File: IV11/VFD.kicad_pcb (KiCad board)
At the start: 2 copper layers, 225 x 80 mm, 71 parts, among them J1 USB_B, SW1 switch, SW2 switch, SW3 switch, SW4 switch, U1 74HC595, U10 UDN2981, U11 UDN2981, U12 UDN2981, U13 WeMos_mini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

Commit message: Changes for back to front LED markings
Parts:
- moved D6 4.07 mm to (154.7, 37.8), turned to 270 degrees
- moved D4 3.96 mm to (98.7, 38.0), turned to 270 degrees
- moved D8 3.96 mm to (211.2, 38.0), turned to 270 degrees
- moved D5 3.95 mm to (126.6, 41.8), turned to 90 degrees
- moved D3 3.81 mm to (70.2, 41.9), turned to 90 degrees
- moved D2 3.81 mm to (42.2, 38.1), turned to 270 degrees
- moved D1 3.78 mm to (14.0, 41.8), turned to 90 degrees
- moved D7 3.49 mm to (182.9, 41.9), turned to 90 degrees
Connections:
- D1 pad 1: LED_DATA_IN -> Net-(D1-Pad1)
- D1 pad 2: Net-(D1-Pad2) -> GND
- D1 pad 3: GND -> Net-(D1-Pad3)
- D1 pad 4: Net-(D1-Pad4) -> LED_DATA_IN
- D2 pad 1: Net-(D1-Pad4) -> Net-(D2-Pad1)
- D2 pad 2: +5V -> Net-(D2-Pad2)
- D2 pad 3: GND -> Net-(D2-Pad3)
- D2 pad 4: Net-(D2-Pad4) -> Net-(D1-Pad1)
- D3 pad 1: Net-(D2-Pad4) -> Net-(D3-Pad1)
- D3 pad 2: +5V -> Net-(D3-Pad2)
- D3 pad 3: GND -> Net-(D3-Pad3)
- D3 pad 4: Net-(D3-Pad4) -> Net-(D2-Pad1)
- D4 pad 1: Net-(D3-Pad4) -> Net-(D4-Pad1)
- D4 pad 2: +5V -> GND
- D4 pad 3: GND -> Net-(D4-Pad3)
- D4 pad 4: Net-(D4-Pad4) -> Net-(D3-Pad1)
- D5 pad 1: Net-(D4-Pad4) -> Net-(D5-Pad1)
- D5 pad 2: +5V -> GND
- D5 pad 3: GND -> +5V
- D5 pad 4: Net-(D5-Pad4) -> Net-(D4-Pad1)
- D6 pad 1: Net-(D5-Pad4) -> Net-(D6-Pad1)
- D6 pad 2: +5V -> Net-(D6-Pad2)
- D6 pad 3: GND -> Net-(D6-Pad3)
- D6 pad 4: Net-(D6-Pad4) -> Net-(D5-Pad1)
- D7 pad 1: Net-(D6-Pad4) -> Net-(D7-Pad1)
- D7 pad 2: +5V -> Net-(D7-Pad2)
- D7 pad 3: GND -> Net-(D7-Pad3)
- D7 pad 4: Net-(D7-Pad4) -> Net-(D6-Pad1)
- D8 pad 1: Net-(D7-Pad4) -> LED_DATA_OUT
- D8 pad 2: +5V -> GND
- D8 pad 3: GND -> Net-(D8-Pad3)
- D8 pad 4: LED_DATA_OUT -> Net-(D7-Pad1)
- D9 pad 1: Net-(D1-Pad2) -> Net-(D1-Pad3)
- SW2 pad 2: GND -> Net-(SW2-Pad2)
- SW3 pad 2: GND -> Net-(SW3-Pad2)
- SW4 pad 2: GND -> Net-(SW4-Pad2)
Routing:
- net Net-(D6-Pad4): track 30.3 -> 0.00 mm
- net Net-(D6-Pad1): track 0.00 -> 30.3 mm
- net Net-(D5-Pad4): track 29.9 -> 0.00 mm
- net Net-(D5-Pad1): track 0.00 -> 29.9 mm
- net Net-(D2-Pad4): track 29.7 -> 0.00 mm
- net Net-(D2-Pad1): track 0.00 -> 29.7 mm
- net Net-(D1-Pad4): track 29.3 -> 0.00 mm
- net Net-(D1-Pad1): track 0.00 -> 29.3 mm
- net Net-(D7-Pad4): track 29.3 -> 0.00 mm
- net Net-(D7-Pad1): track 0.00 -> 29.3 mm
- net Net-(D3-Pad4): track 29.1 -> 0.00 mm
- net Net-(D3-Pad1): track 0.00 -> 29.1 mm
- net Net-(D4-Pad4): track 29.1 -> 0.00 mm
- net Net-(D4-Pad1): track 0.00 -> 29.1 mm
- net Net-(D1-Pad3): track 0.00 -> 14.8 mm, vias 0 -> 1
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
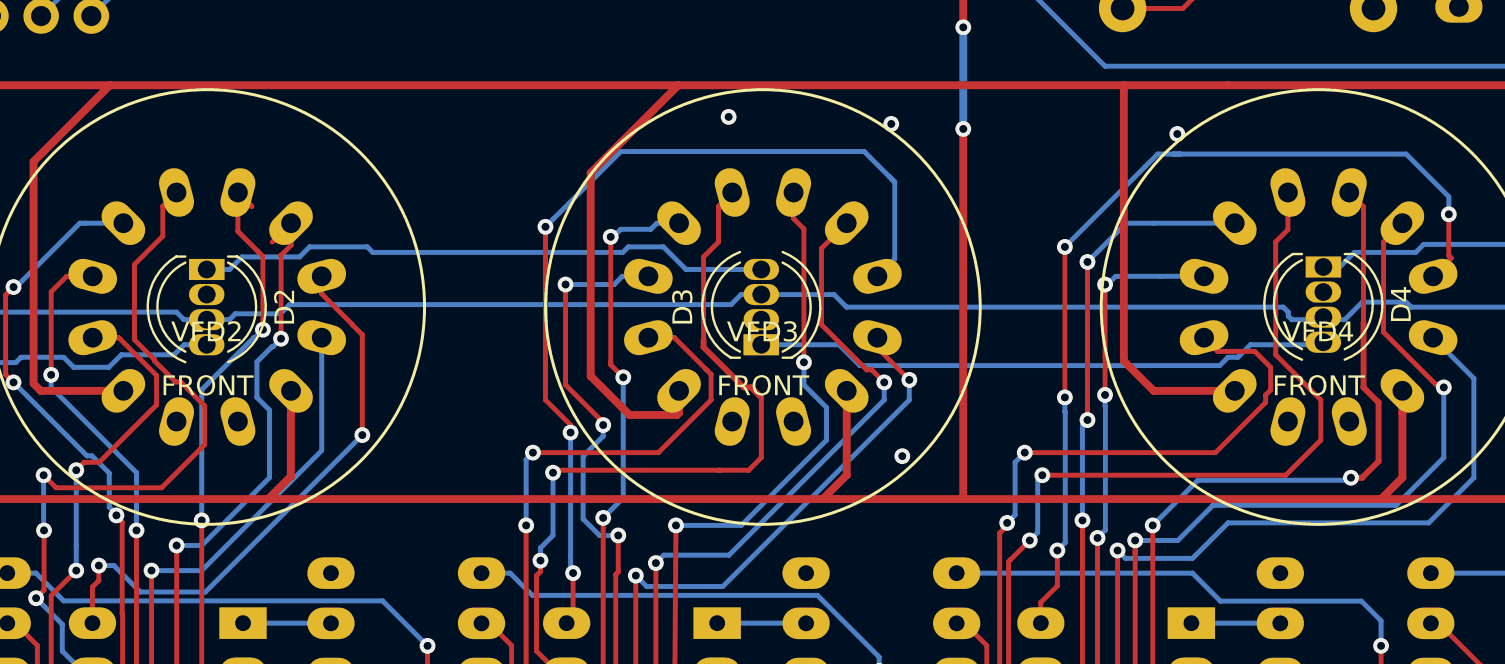
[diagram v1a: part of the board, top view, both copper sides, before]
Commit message: Fix footpring mistakes
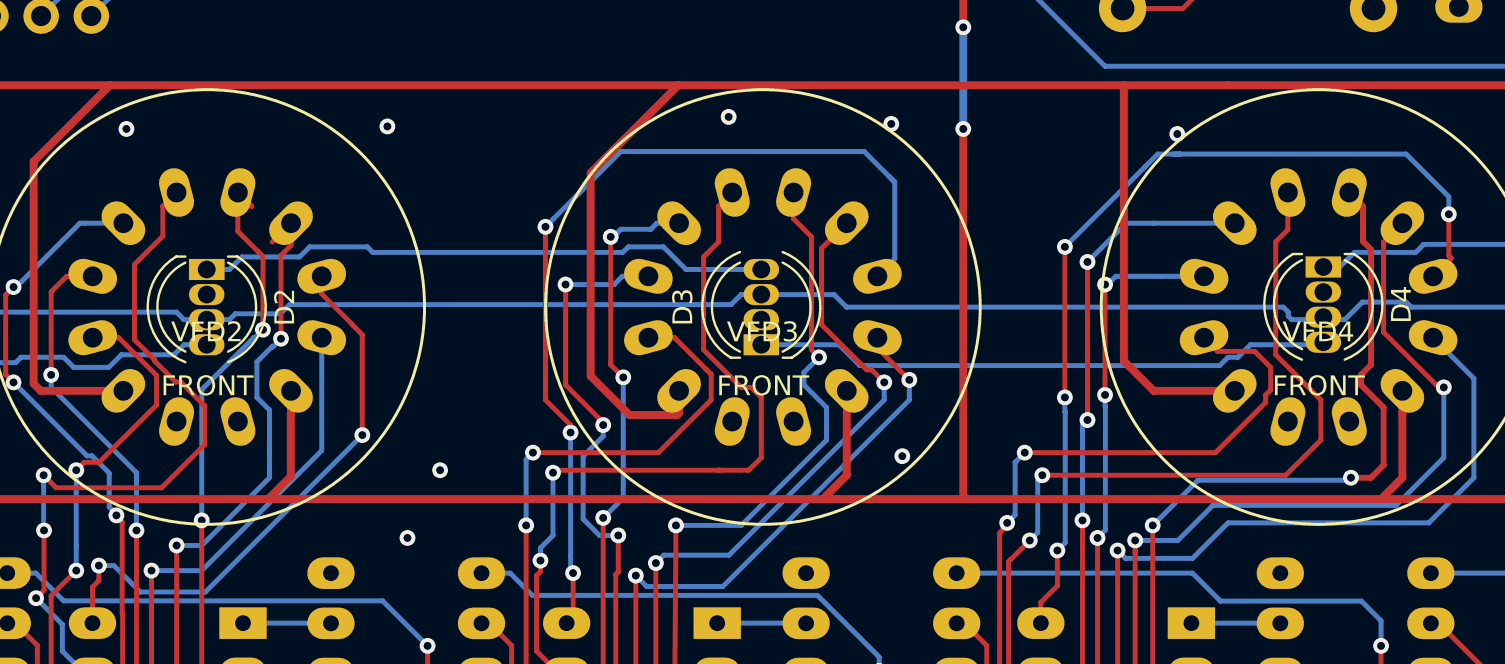
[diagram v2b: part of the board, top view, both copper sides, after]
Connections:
- C1 pad 1: VCC -> +3V3
- C2 pad 1: VCC -> +3V3
- C3 pad 1: VCC -> +3V3
- C4 pad 1: VCC -> +3V3
- C5 pad 1: VCC -> +3V3
- C6 pad 1: VCC -> +3V3
- C7 pad 1: VCC -> +3V3
- C8 pad 1: VCC -> +3V3
- D3 pad 2: Net-(D3-Pad2) -> GND
- D3 pad 3: Net-(D3-Pad3) -> +5V
- D4 pad 3: Net-(D4-Pad3) -> +5V
- D6 pad 2: Net-(D6-Pad2) -> GND
- D6 pad 3: Net-(D6-Pad3) -> +5V
- U1 pad 10: VCC -> +3V3
- U1 pad 16: VCC -> +3V3
- U14 pad 10: VCC -> +3V3
- U14 pad 16: VCC -> +3V3
- U15 pad 10: VCC -> +3V3
- U15 pad 16: VCC -> +3V3
- U2 pad 10: VCC -> +3V3
- U2 pad 16: VCC -> +3V3
- U3 pad 10: VCC -> +3V3
- U3 pad 16: VCC -> +3V3
- U7 pad 10: VCC -> +3V3
- U7 pad 16: VCC -> +3V3
- U8 pad 10: VCC -> +3V3
- U8 pad 16: VCC -> +3V3
- U9 pad 10: VCC -> +3V3
- U9 pad 16: VCC -> +3V3
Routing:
- net VCC: track 411.5 -> 0.00 mm
- net +3V3: track 260.0 -> 671.4 mm
- net Net-(U5-Pad11): track 49.4 -> 51.4 mm
- net Net-(U11-Pad11): track 52.9 -> 53.8 mm
- net GND: vias 19 -> 23

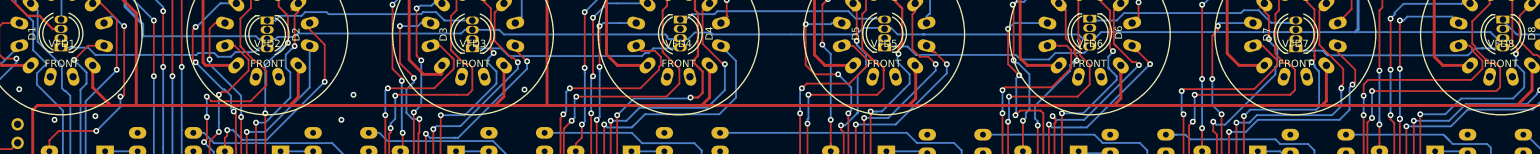
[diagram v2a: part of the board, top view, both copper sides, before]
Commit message: Update footprints to use the 'generic modules'
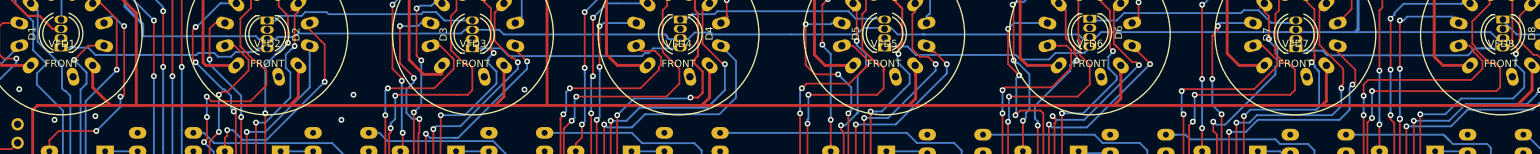
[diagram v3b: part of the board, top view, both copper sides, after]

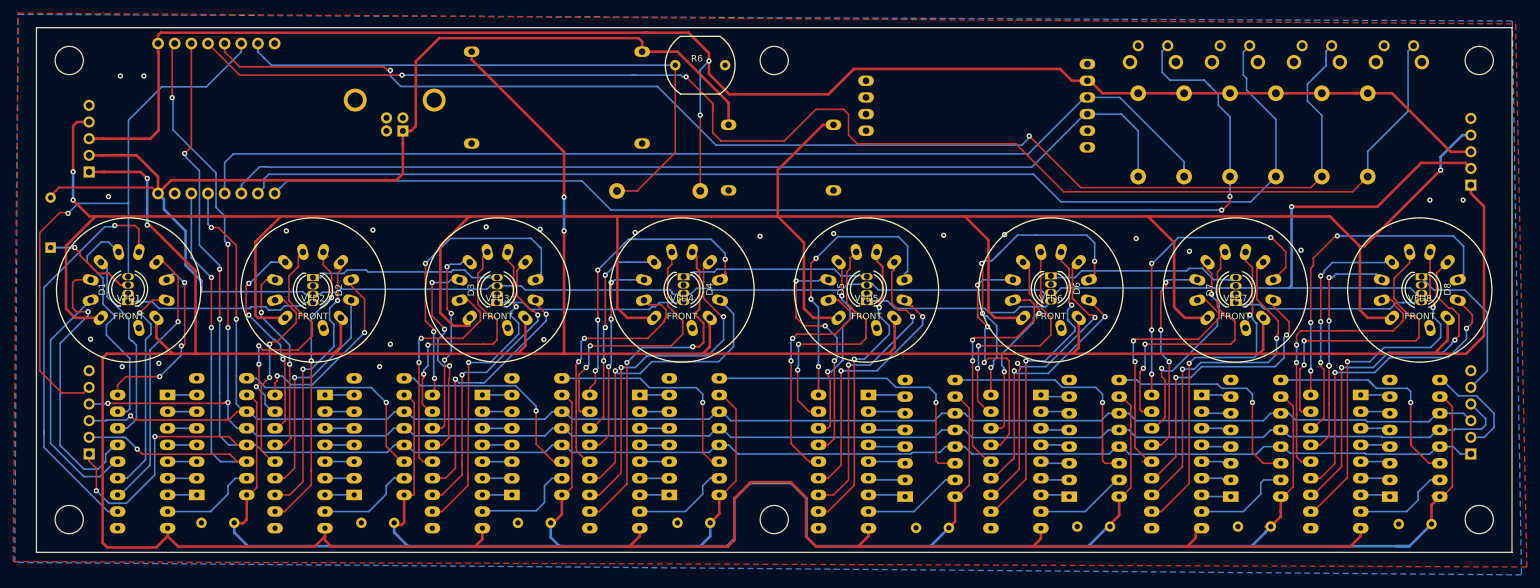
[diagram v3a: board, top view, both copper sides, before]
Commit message: Finish import of new neopixel footprint and associated groundfill changes
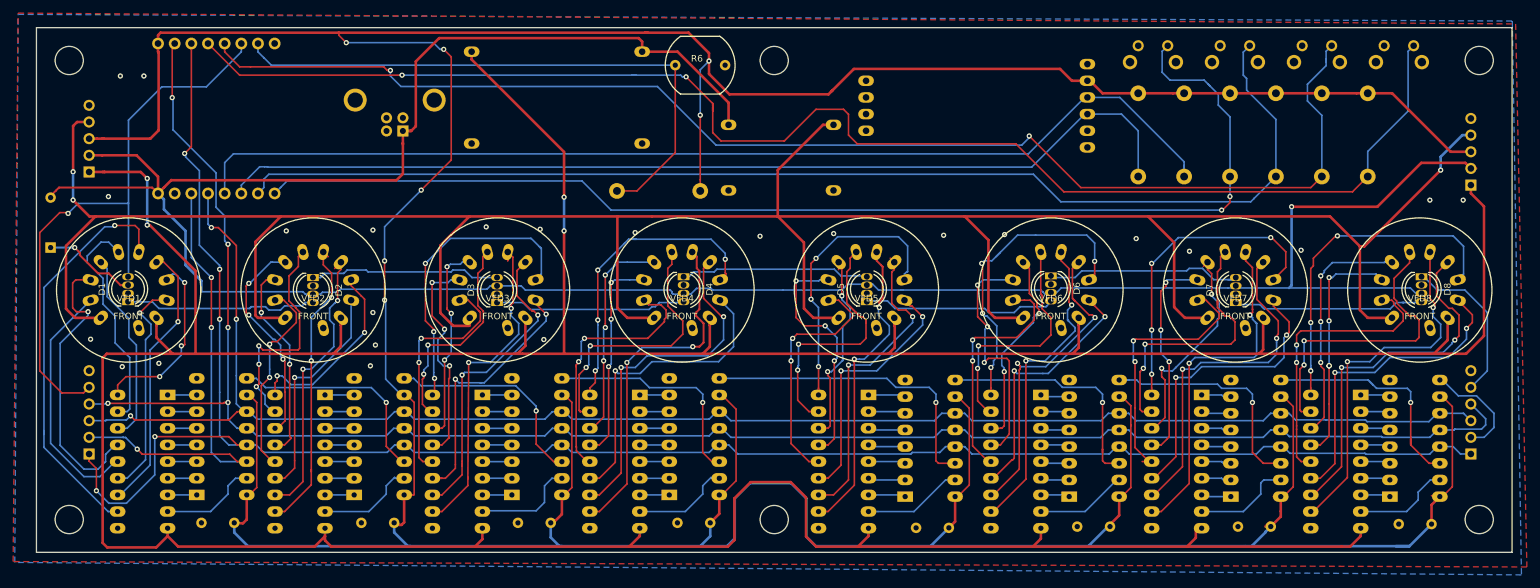
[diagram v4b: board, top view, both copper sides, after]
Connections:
- D2 pad 2: Net-(D2-Pad2) -> GND
- D2 pad 3: Net-(D2-Pad3) -> +5V
- D7 pad 2: Net-(D7-Pad2) -> GND
- D7 pad 3: Net-(D7-Pad3) -> +5V
- D8 pad 3: Net-(D8-Pad3) -> +5V
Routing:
- net +3V3: track 671.4 -> 747.6 mm, vias 2 -> 7
- net Net-(U5-Pad17): track 37.9 -> 33.1 mm
- net Net-(U10-Pad17): track 36.2 -> 34.5 mm
- net Net-(U4-Pad17): track 35.4 -> 34.3 mm
- net Net-(U5-Pad11): track 51.4 -> 52.4 mm
- net GND: vias 23 -> 24

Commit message: Updates to use further-spaced LED footprints for the 5mm neopixels to make rework easier!
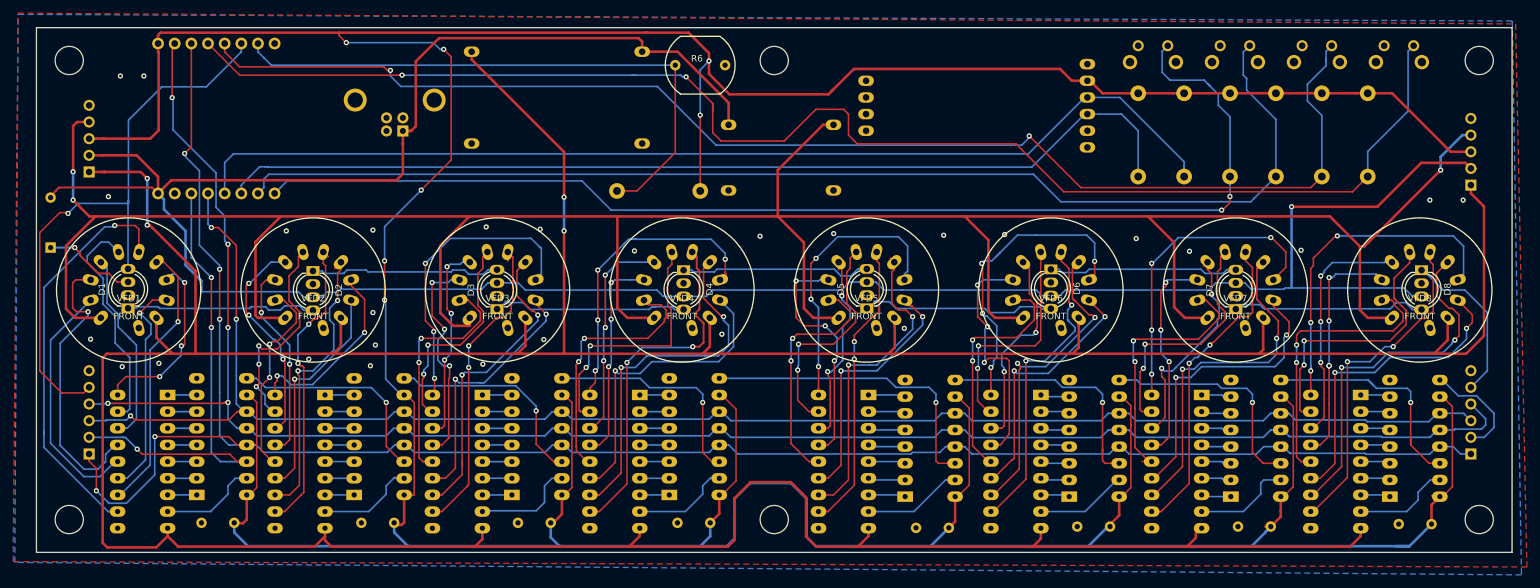
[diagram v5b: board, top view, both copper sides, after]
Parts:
- D1, D2, D3, D4, D5, D6, D7, D8: footprint LED_THT:LED_D5.0mm-4 -> 5mm-neopixel-wide:LED_D5.0mm-4-Wide
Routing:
- net Net-(U16-Pad11): track 53.6 -> 48.4 mm
- net Net-(U16-Pad17): track 42.1 -> 37.3 mm
- net Net-(U17-Pad17): track 46.4 -> 42.4 mm
- net Net-(U6-Pad17): track 39.7 -> 35.8 mm
- net Net-(U17-Pad11): track 55.1 -> 52.3 mm
- net +5V: track 400.0 -> 402.5 mm
- net Net-(U5-Pad11): track 52.4 -> 50.2 mm
- net Net-(U10-Pad17): track 34.5 -> 32.4 mm
- net Net-(U6-Pad11): track 47.2 -> 45.3 mm
- net Net-(U11-Pad12): track 53.4 -> 55.4 mm
- net Net-(U12-Pad17): track 36.2 -> 34.5 mm
- net Net-(U11-Pad17): track 40.9 -> 39.5 mm
- net Net-(D6-Pad1): track 30.3 -> 29.1 mm
- net LED_DATA_IN: track 92.5 -> 91.7 mm
- net Net-(D3-Pad1): track 29.1 -> 29.9 mm
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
